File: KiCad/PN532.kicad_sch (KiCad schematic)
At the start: 57 parts, among them J1 Bell, J2 Header, J3 SPOX, SW1 TAMPER, U1 PN532, U2 QR, U3 QR, Y1 27.12MHz

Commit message: Part numbers
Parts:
- C1, C10, C11, C12, C13, C14, C15, C16, C17, C18, C19, C2, C3, C4, C5, C6, C7, C8, C9, R10, R11, R12, R13, R14, R4, R5, R6, R7, R9: Note (none) -> 0603
- D1, D2, D3: Note (none) -> 0603 mounted face down
- J1, J2, J3: Note (none) -> Non fit
- R15: Notye (none) -> 0603

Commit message: Fabrication files
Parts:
- A1, AJK1, AJK2, H1, H2, JP1, TP1, U2, U3: Note (none) -> No part, PCB printed
- R15: Note (none) -> 0603; Notye 0603 -> (none)
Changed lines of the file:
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@@
+      (effects (font (size 1.27 1.27)) hide)
+    )
+    (property "Note" "No part, PCB printed" (id 4) (at 34.29 102.87 0)
       (effects (font (size 1.27 1.27)) hide)
     )
@@
       (effects (font (size 1.27 1.27)) hide)
     )
+    (property "Note" "No part, PCB printed" (id 4) (at 243.84 35.56 0)
+      (effects (font (size 1.27 1.27)) hide)
+    )
   )
   (symbol (lib_id "Mechanical:MountingHole") (at 243.84 41.91 0) (unit 1)
@@
     )
     (property "Datasheet" "~" (id 3) (at 243.84 41.91 0)
+      (effects (font (size 1.27 1.27)) hide)
+    )
+    (property "Note" "No part, PCB printed" (id 4) (at 243.84 41.91 0)
       (effects (font (size 1.27 1.27)) hide)
     )
@@
       (effects (font (size 1.27 1.27)) hide)
     )
+    (property "Note" "No part, PCB printed" (id 4) (at 268.605 173.355 0)
+      (effects (font (size 1.27 1.27)) hide)
+    )
   )
   (symbol (lib_id "Device:R") (at 228.6 20.32 270) (unit 1)
@@
       (effects (font (size 1.27 1.27)) hide)
     )
+    (property "Note" "No part, PCB printed" (id 4) (at 281.305 173.355 0)
+      (effects (font (size 1.27 1.27)) hide)
+    )
   )
   (symbol (lib_id "Device:R") (at 250.19 152.4 270) (unit 1)
@@
       (effects (font (size 1.27 1.27)) hide)
     )
-    (property "Notye" "0603" (id 4) (at 250.19 152.4 90)
+    (property "Note" "0603" (id 4) (at 250.19 152.4 90)
       (effects (font (size 1.27 1.27)) hide)
     )
@@
     )
     (property "Datasheet" "~" (id 3) (at 193.04 148.59 0)
+      (effects (font (size 1.27 1.27)) hide)
+    )
+    (property "Note" "No part, PCB printed" (id 4) (at 193.04 148.59 90)
       (effects (font (size 1.27 1.27)) hide)
     )
@@
       (effects (font (size 1.27 1.27)) hide)
     )
+    (property "Note" "No part, PCB printed" (id 4) (at 109.22 102.87 90)
+      (effects (font (size 1.27 1.27)) hide)
+    )
     (pin "1")
     (pin "2")
@@
       (effects (font (size 1.27 1.27)) hide)
     )
+    (property "Note" "No part, PCB printed" (id 4) (at 276.86 173.355 0)
+      (effects (font (size 1.27 1.27)) hide)
+    )
   )
   (symbol (lib_id "RevK:AJK") (at 264.16 173.355 0) (unit 1)
@@
       (effects (font (size 1.27 1.27)) hide)
     )
+    (property "Note" "No part, PCB printed" (id 4) (at 264.16 173.355 0)
+      (effects (font (size 1.27 1.27)) hide)
+    )

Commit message: BOM tidy
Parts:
- A1, AJK1, AJK2, U2, U3: Note No part, PCB printed -> Non part, PCB printed; now left out of the parts list
- C1, C2: Note 0603 -> (none)
- H1, H2, J1, J2, J3, JP1, TP1: now left out of the parts list
- R8: Note (none) -> 0603
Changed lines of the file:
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@@
   )
   (symbol (lib_id "RevK:PN532-Antenna") (at 34.29 102.87 0) (unit 1)
-    (in_bom yes) (on_board yes)
+    (in_bom no) (on_board yes)
     (property "Reference" "A1" (id 0) (at 35.7632 85.979 0))
     (property "Value" "PN532-Antenna" (id 1) (at 35.7632 88.2904 0))
@@
       (effects (font (size 1.27 1.27)) hide)
     )
-    (property "Note" "No part, PCB printed" (id 4) (at 34.29 102.87 0)
+    (property "Note" "Non part, PCB printed" (id 4) (at 34.29 102.87 0)
       (effects (font (size 1.27 1.27)) hide)
     )
@@
     (pin "9")
   )
-  (symbol (lib_id "RevK:Cx2") (at 64.77 97.79 0) (unit 1)
+  (symbol (lib_name "Cx2_1") (lib_id "RevK:Cx2") (at 64.77 97.79 0) (unit 1)
     (in_bom yes) (on_board yes)
     (property "Reference" "C1" (id 0) (at 59.69 97.79 0)
@@
       (effects (font (size 1.27 1.27)) hide)
     )
-    (property "Note" "0603" (id 4) (at 64.77 97.79 0)
+    (property "Note" "" (id 4) (at 64.77 97.79 0)
       (effects (font (size 1.27 1.27)) hide)
     )
@@
       (effects (font (size 1.27 1.27)) hide)
     )
-    (property "Note" "0603" (id 4) (at 64.77 107.95 0)
+    (property "Note" "" (id 4) (at 64.77 107.95 0)
       (effects (font (size 1.27 1.27)) hide)
     )
@@
     (pin "1")
   )
-  (symbol (lib_id "Mechanical:MountingHole") (at 243.84 35.56 0) (unit 1)
-    (in_bom yes) (on_board yes)
+  (symbol (lib_name "MountingHole_1") (lib_id "Mechanical:MountingHole") (at 243.84 35.56 0) (unit 1)
+    (in_bom no) (on_board yes)
     (property "Reference" "H1" (id 0) (at 246.38 34.3916 0)
       (effects (font (size 1.27 1.27)) (justify left) hide)
@@
   )
   (symbol (lib_id "Mechanical:MountingHole") (at 243.84 41.91 0) (unit 1)
-    (in_bom yes) (on_board yes)
+    (in_bom no) (on_board yes)
     (property "Reference" "H2" (id 0) (at 246.38 40.7416 0)
       (effects (font (size 1.27 1.27)) (justify left) hide)
@@
   )
   (symbol (lib_id "Connector:Conn_01x04_Male") (at 247.65 62.23 0) (unit 1)
-    (in_bom yes) (on_board yes)
+    (in_bom no) (on_board yes)
     (property "Reference" "J2" (id 0) (at 250.3932 55.0926 0))
     (property "Value" "Header" (id 1) (at 250.3932 57.404 0))
@@
   )
   (symbol (lib_id "Connector:Conn_01x04_Male") (at 247.65 78.74 0) (unit 1)
-    (in_bom yes) (on_board yes)
+    (in_bom no) (on_board yes)
     (property "Reference" "J3" (id 0) (at 250.3932 71.6026 0))
     (property "Value" "SPOX" (id 1) (at 250.3932 73.914 0))
@@
   )
   (symbol (lib_id "power:+5V") (at 252.73 62.23 270) (unit 1)
-    (in_bom yes) (on_board yes)
+    (in_bom no) (on_board yes)
     (property "Reference" "#PWR042" (id 0) (at 248.92 62.23 0)
       (effects (font (size 1.27 1.27)) hide)
@@
       (effects (font (size 1.27 1.27)) hide)
     )
-    (property "Datasheet" "~" (id 3) (at 213.36 30.48 0)
+    (property "Datasheet" "https://www.mouser.co.uk/ProductDetail/603-AC0603JR-07470RL" (id 3) (at 213.36 30.48 0)
+      (effects (font (size 1.27 1.27)) hide)
+    )
+    (property "Note" "0603" (id 4) (at 213.36 30.48 90)
       (effects (font (size 1.27 1.27)) hide)
     )
@@
     (pin "2")
   )
-  (symbol (lib_id "RevK:AJK") (at 268.605 173.355 0) (unit 1)
-    (in_bom yes) (on_board yes)
+  (symbol (lib_name "AJK_1") (lib_id "RevK:AJK") (at 268.605 173.355 0) (unit 1)
+    (in_bom no) (on_board yes)
     (property "Reference" "AJK2" (id 0) (at 268.605 170.815 0)
       (effects (font (size 1.27 1.27)) hide)
@@
       (effects (font (size 1.27 1.27)) hide)
     )
-    (property "Note" "No part, PCB printed" (id 4) (at 268.605 173.355 0)
+    (property "Note" "Non part, PCB printed" (id 4) (at 268.605 173.355 0)
       (effects (font (size 1.27 1.27)) hide)
     )
@@
   )
   (symbol (lib_id "Connector:Conn_01x02_Male") (at 212.09 149.86 0) (unit 1)
-    (in_bom yes) (on_board yes)
+    (in_bom no) (on_board yes)
     (property "Reference" "J1" (id 0) (at 214.8332 145.2626 0))
     (property "Value" "Bell" (id 1) (at 214.8332 147.574 0))
@@
   )
   (symbol (lib_id "RevK:QR") (at 281.305 173.355 0) (unit 1)
-    (in_bom yes) (on_board yes)
+    (in_bom no) (on_board yes)
     (property "Reference" "U3" (id 0) (at 281.305 174.625 0)
       (effects (font (size 1.27 1.27)) hide)
@@
       (effects (font (size 1.27 1.27)) hide)
     )
-    (property "Note" "No part, PCB printed" (id 4) (at 281.305 173.355 0)
+    (property "Note" "Non part, PCB printed" (id 4) (at 281.305 173.355 0)
       (effects (font (size 1.27 1.27)) hide)
     )
@@
   )
   (symbol (lib_id "Jumper:SolderJumper_3_Bridged12") (at 193.04 148.59 270) (mirror x) (unit 1)
-    (in_bom yes) (on_board yes)
+    (in_bom no) (on_board yes)
     (property "Reference" "JP1" (id 0) (at 194.7672 147.4216 90)
       (effects (font (size 1.27 1.27)) (justify left))
@@
   )
   (symbol (lib_id "Connector:TestPoint_2Pole") (at 109.22 102.87 270) (unit 1)
-    (in_bom yes) (on_board yes)
+    (in_bom no) (on_board yes)
     (property "Reference" "TP1" (id 0) (at 110.6932 101.7016 90)
       (effects (font (size 1.27 1.27)) (justify left))
@@
     (pin "1")
   )
-  (symbol (lib_id "RevK:QR") (at 276.86 173.355 0) (unit 1)
-    (in_bom yes) (on_board yes)
+  (symbol (lib_name "QR_1") (lib_id "RevK:QR") (at 276.86 173.355 0) (unit 1)
+    (in_bom no) (on_board yes)
     (property "Reference" "U2" (id 0) (at 276.86 174.625 0)
       (effects (font (size 1.27 1.27)) hide)
@@
       (effects (font (size 1.27 1.27)) hide)
     )
-    (property "Note" "No part, PCB printed" (id 4) (at 276.86 173.355 0)
+    (property "Note" "Non part, PCB printed" (id 4) (at 276.86 173.355 0)
       (effects (font (size 1.27 1.27)) hide)
     )
   )
   (symbol (lib_id "RevK:AJK") (at 264.16 173.355 0) (unit 1)
-    (in_bom yes) (on_board yes)
+    (in_bom no) (on_board yes)
     (property "Reference" "AJK1" (id 0) (at 264.16 170.815 0)
       (effects (font (size 1.27 1.27)) hide)
@@
       (effects (font (size 1.27 1.27)) hide)
     )
-    (property "Note" "No part, PCB printed" (id 4) (at 264.16 173.355 0)
-      (effects (font (size 1.27 1.27)) hide)
-    )
-  )
-  (symbol (lib_id "RevK:Hidden") (at 52.705 100.33 0) (unit 1)
+    (property "Note" "Non part, PCB printed" (id 4) (at 264.16 173.355 0)
+      (effects (font (size 1.27 1.27)) hide)
+    )
+  )
+  (symbol (lib_name "Hidden_2") (lib_id "RevK:Hidden") (at 52.705 100.33 0) (unit 1)
     (in_bom yes) (on_board yes)
     (property "Reference" "R1" (id 0) (at 53.34 100.33 0)
@@
       (effects (font (size 1.27 1.27)) hide)
     )
-    (property "Datasheet" "" (id 3) (at 52.705 102.87 0)
+    (property "Datasheet" "https://www.mouser.co.uk/ProductDetail/603-RC0603FR-102K7L" (id 3) (at 52.705 102.87 0)
       (effects (font (size 1.27 1.27)) hide)
     )
@@
     (pin "~")
   )
-  (symbol (lib_id "RevK:Hidden") (at 52.705 105.41 0) (unit 1)
+  (symbol (lib_name "Hidden_1") (lib_id "RevK:Hidden") (at 52.705 105.41 0) (unit 1)
     (in_bom yes) (on_board yes)
     (property "Reference" "R3" (id 0) (at 53.34 105.41 0)

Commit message: More bom/pos tidy
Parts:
- C1, C2: value 160pF -> 160pF 1%
- C3, C4: value 22pF -> 22pF 1%
- C8: value 1nF -> 1nF 2%
- L1, L2: Note (none) -> High quality inductor
- R4: value 2K7 -> 2K7 1%
- R5: value 1K -> 1K 1%
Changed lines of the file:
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@@
       (effects (font (size 1.27 1.27)) (justify left))
     )
-    (property "Value" "160pF" (id 1) (at 58.42 95.25 0)
+    (property "Value" "160pF 1%" (id 1) (at 58.42 95.25 0)
       (effects (font (size 1.27 1.27)) (justify left))
     )
@@
       (effects (font (size 1.27 1.27)) (justify left))
     )
-    (property "Value" "160pF" (id 1) (at 58.42 110.49 0)
+    (property "Value" "160pF 1%" (id 1) (at 58.42 110.49 0)
       (effects (font (size 1.27 1.27)) (justify left))
     )
@@
     (in_bom yes) (on_board yes)
     (property "Reference" "C3" (id 0) (at 76.2 86.3092 90))
-    (property "Value" "22pF" (id 1) (at 76.2 88.6206 90))
+    (property "Value" "22pF 1%" (id 1) (at 76.2 88.6206 90))
     (property "Footprint" "RevK:C_0603" (id 2) (at 72.39 93.6752 0)
       (effects (font (size 1.27 1.27)) hide)
@@
     (in_bom yes) (on_board yes)
     (property "Reference" "C4" (id 0) (at 76.2 119.4308 90))
-    (property "Value" "22pF" (id 1) (at 76.2 117.1194 90))
+    (property "Value" "22pF 1%" (id 1) (at 76.2 117.1194 90))
     (property "Footprint" "RevK:C_0603" (id 2) (at 80.01 112.0648 0)
       (effects (font (size 1.27 1.27)) hide)
@@
       (effects (font (size 1.27 1.27)) hide)
     )
+    (property "Note" "High quality inductor" (id 4) (at 99.06 92.71 90)
+      (effects (font (size 1.27 1.27)) hide)
+    )
     (pin "1")
     (pin "2")
@@
       (effects (font (size 1.27 1.27)) hide)
     )
+    (property "Note" "High quality inductor" (id 4) (at 99.06 113.03 90)
+      (effects (font (size 1.27 1.27)) hide)
+    )
     (pin "1")
     (pin "2")
@@
     (in_bom yes) (on_board yes)
     (property "Reference" "C8" (id 0) (at 111.76 132.08 90))
-    (property "Value" "1nF" (id 1) (at 111.76 122.9106 90))
+    (property "Value" "1nF 2%" (id 1) (at 111.76 122.9106 90))
     (property "Footprint" "RevK:C_0603" (id 2) (at 107.95 127.9652 0)
       (effects (font (size 1.27 1.27)) hide)
@@
     (in_bom yes) (on_board yes)
     (property "Reference" "R4" (id 0) (at 101.6 132.08 90))
-    (property "Value" "2K7" (id 1) (at 101.6 124.0536 90))
+    (property "Value" "2K7 1%" (id 1) (at 101.6 124.0536 90))
     (property "Footprint" "RevK:R_0603" (id 2) (at 101.6 125.222 90)
       (effects (font (size 1.27 1.27)) hide)
@@
       (effects (font (size 1.27 1.27)) (justify right))
     )
-    (property "Value" "1K" (id 1) (at 130.048 124.333 0)
+    (property "Value" "1K 1%" (id 1) (at 130.048 124.333 0)
       (effects (font (size 1.27 1.27)) (justify right))
     )
@@
     )
     (path "/00000000-0000-0000-0000-000060756cae"
-      (reference "C1") (unit 1) (value "160pF") (footprint "RevK:Cx2_0603")
+      (reference "C1") (unit 1) (value "160pF 1%") (footprint "RevK:Cx2_0603")
     )
     (path "/00000000-0000-0000-0000-000060757e92"
-      (reference "C2") (unit 1) (value "160pF") (footprint "RevK:Cx2_0603")
+      (reference "C2") (unit 1) (value "160pF 1%") (footprint "RevK:Cx2_0603")
     )
     (path "/00000000-0000-0000-0000-000060758ce7"
-      (reference "C3") (unit 1) (value "22pF") (footprint "RevK:C_0603")
+      (reference "C3") (unit 1) (value "22pF 1%") (footprint "RevK:C_0603")
     )
     (path "/00000000-0000-0000-0000-000060759861"
-      (reference "C4") (unit 1) (value "22pF") (footprint "RevK:C_0603")
+      (reference "C4") (unit 1) (value "22pF 1%") (footprint "RevK:C_0603")
     )
     (path "/00000000-0000-0000-0000-00006075a7aa"
@@
     )
     (path "/00000000-0000-0000-0000-00006075c646"
-      (reference "C8") (unit 1) (value "1nF") (footprint "RevK:C_0603")
+      (reference "C8") (unit 1) (value "1nF 2%") (footprint "RevK:C_0603")
     )
     (path "/00000000-0000-0000-0000-00006075d8ac"
@@
     )
     (path "/00000000-0000-0000-0000-00006075de03"
-      (reference "R4") (unit 1) (value "2K7") (footprint "RevK:R_0603")
+      (reference "R4") (unit 1) (value "2K7 1%") (footprint "RevK:R_0603")
     )
     (path "/00000000-0000-0000-0000-00006075e871"
-      (reference "R5") (unit 1) (value "1K") (footprint "RevK:R_0603")
+      (reference "R5") (unit 1) (value "1K 1%") (footprint "RevK:R_0603")
     )
     (path "/00000000-0000-0000-0000-000060762055"

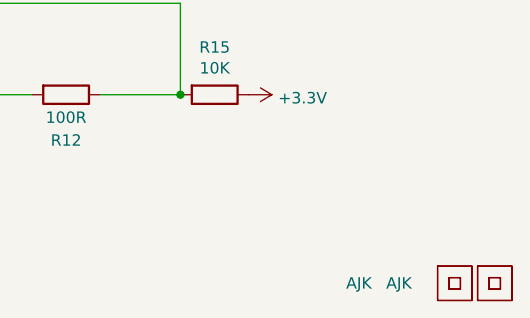
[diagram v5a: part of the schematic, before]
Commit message: Mostly cosmetic changes and a few track tweaks
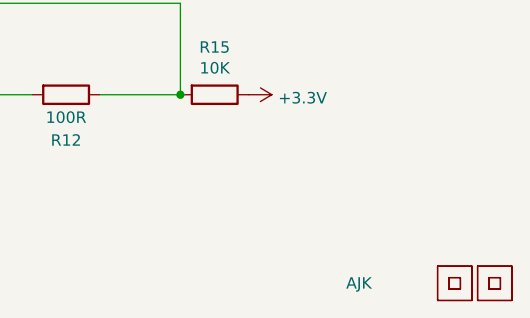
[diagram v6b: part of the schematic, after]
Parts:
- removed AJK2: AJK, RevK:AJK, symbol RevK:AJK
- A1: footprint RevK:PN532-Antenna4 -> RevK:PN532-Antenna5
- J2: footprint Connector_PinHeader_2.54mm:PinHeader_1x04_P2.54mm_Vertical -> RevK:PinHeader_1x04_P2.54mm_Vertical
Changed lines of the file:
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@@
     (property "Reference" "A1" (id 0) (at 35.7632 85.979 0))
     (property "Value" "PN532-Antenna" (id 1) (at 35.7632 88.2904 0))
-    (property "Footprint" "RevK:PN532-Antenna4" (id 2) (at 34.29 102.87 0)
+    (property "Footprint" "RevK:PN532-Antenna5" (id 2) (at 34.29 102.87 0)
       (effects (font (size 1.27 1.27)) hide)
     )
@@
     (property "Reference" "J2" (id 0) (at 250.3932 55.0926 0))
     (property "Value" "Header" (id 1) (at 250.3932 57.404 0))
-    (property "Footprint" "Connector_PinHeader_2.54mm:PinHeader_1x04_P2.54mm_Vertical" (id 2) (at 247.65 62.23 0)
+    (property "Footprint" "RevK:PinHeader_1x04_P2.54mm_Vertical" (id 2) (at 247.65 62.23 0)
       (effects (font (size 1.27 1.27)) hide)
     )
@@
     (pin "2")
   )
-  (symbol (lib_name "AJK_1") (lib_id "RevK:AJK") (at 268.605 173.355 0) (unit 1)
-    (in_bom no) (on_board yes)
-    (property "Reference" "AJK2" (id 0) (at 268.605 170.815 0)
-      (effects (font (size 1.27 1.27)) hide)
-    )
-    (property "Value" "AJK" (id 1) (at 269.24 173.355 0)
-      (effects (font (size 1.27 1.27)) (justify left))
-    )
-    (property "Footprint" "RevK:AJK" (id 2) (at 268.605 175.895 0)
-      (effects (font (size 1.27 1.27)) hide)
-    )
-    (property "Datasheet" "" (id 3) (at 268.605 175.895 0)
-      (effects (font (size 1.27 1.27)) hide)
-    )
-    (property "Note" "Non part, PCB printed" (id 4) (at 268.605 173.355 0)
-      (effects (font (size 1.27 1.27)) hide)
-    )
-  )
   (symbol (lib_id "Device:R") (at 228.6 20.32 270) (unit 1)
     (in_bom yes) (on_board yes)
@@
     )
     (path "/00000000-0000-0000-0000-00006074e4ec"
-      (reference "A1") (unit 1) (value "PN532-Antenna") (footprint "RevK:PN532-Antenna4")
+      (reference "A1") (unit 1) (value "PN532-Antenna") (footprint "RevK:PN532-Antenna5")
     )
     (path "/00000000-0000-0000-0000-00006185d41b"
       (reference "AJK1") (unit 1) (value "AJK") (footprint "RevK:AJK")
     )
-    (path "/00000000-0000-0000-0000-0000607f5b4a"
-      (reference "AJK2") (unit 1) (value "AJK") (footprint "RevK:AJK")
-    )
     (path "/00000000-0000-0000-0000-000060756cae"
       (reference "C1") (unit 1) (value "160pF 1%") (footprint "RevK:Cx2_0603")
@@
     )
     (path "/00000000-0000-0000-0000-0000607d09fb"
-      (reference "J2") (unit 1) (value "Header") (footprint "Connector_PinHeader_2.54mm:PinHeader_1x04_P2.54mm_Vertical")
+      (reference "J2") (unit 1) (value "Header") (footprint "RevK:PinHeader_1x04_P2.54mm_Vertical")
     )
     (path "/00000000-0000-0000-0000-0000607d486c"
